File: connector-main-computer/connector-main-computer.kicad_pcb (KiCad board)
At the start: 2 copper layers, 97.3 x 100.3 mm, 42 parts, among them J1 DVI-I_Dual_Link, J10 Conn_01x04_MountingPin, J11 Conn_01x04_MountingPin, J12 Conn_01x02_MountingPin, J13 Conn_01x04_MountingPin, J2 Conn_01x03_MountingPin, J3 Conn_01x03_MountingPin, J4 Conn_01x03_MountingPin, J5 Conn_01x03_MountingPin, J6 Conn_01x03_MountingPin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

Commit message: add current divider
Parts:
- added R7: R, Resistor_SMD:R_0805_2012Metric, F.Cu at (121.9, 116.4)
- added R8: R, Resistor_SMD:R_0805_2012Metric, F.Cu at (121.9, 121.9)
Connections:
- J6 pad 1: TEST_STAND_BAT_V -> Net-(J6-Pin_1)
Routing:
- net Net-(J6-Pin_1): track 0.00 -> 10.3 mm
- net TEST_STAND_BAT_V: track 83.4 -> 76.4 mm
- net GND: track 245.0 -> 246.1 mm, vias 30 -> 31

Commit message: change strain power supply
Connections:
- J1 pad 9: +12V -> GND
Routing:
- net +12V: track 238.9 -> 236.6 mm
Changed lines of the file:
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@@
 			(layers "*.Cu" "*.Mask")
 			(remove_unused_layers no)
-			(net 3 "+12V")
+			(net 1 "GND")
 			(pinfunction "D1-")
 			(pintype "passive")
@@
 	)
 	(segment
-		(start 95.3008 53.8988)
-		(end 94.8944 53.8988)
-		(width 1)
-		(layer "B.Cu")
-		(net 3)
-	)
-	(segment
 		(start 58.166 61.8236)
 		(end 68.6816 61.8236)
@@
 	)
 	(segment
-		(start 94.8944 53.8988)
-		(end 94.4032 54.39)
-		(width 1)
-		(layer "B.Cu")
-		(net 3)
-	)
-	(segment
 		(start 95.3008 53.8988)
 		(end 95.3008 55.6768)
@@
 		(width 1)
 		(layer "B.Cu")
-		(net 3)
-	)
-	(segment
-		(start 94.4032 54.39)
-		(end 93.218 54.39)
-		(width 1)
-		(layer "B.Cu")

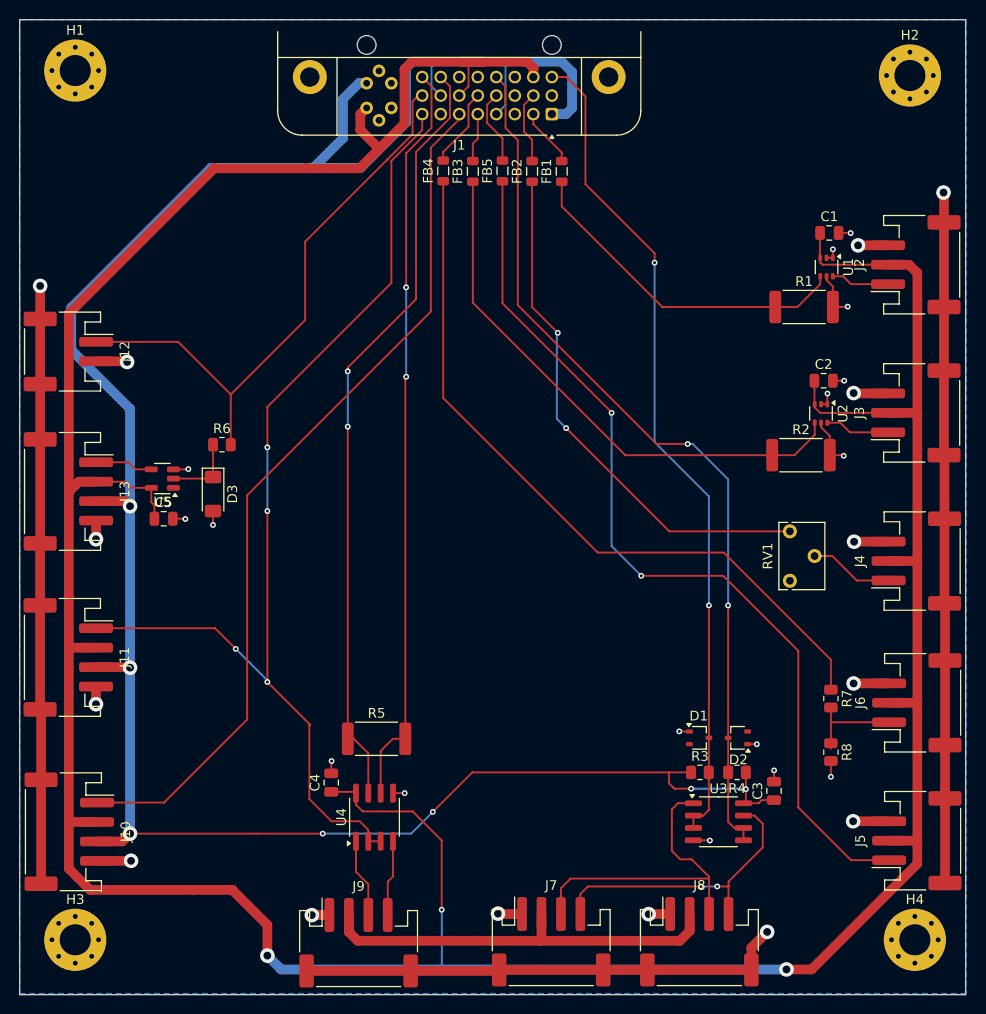
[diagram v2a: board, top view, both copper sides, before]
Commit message: Connector main computer texts and move connectors
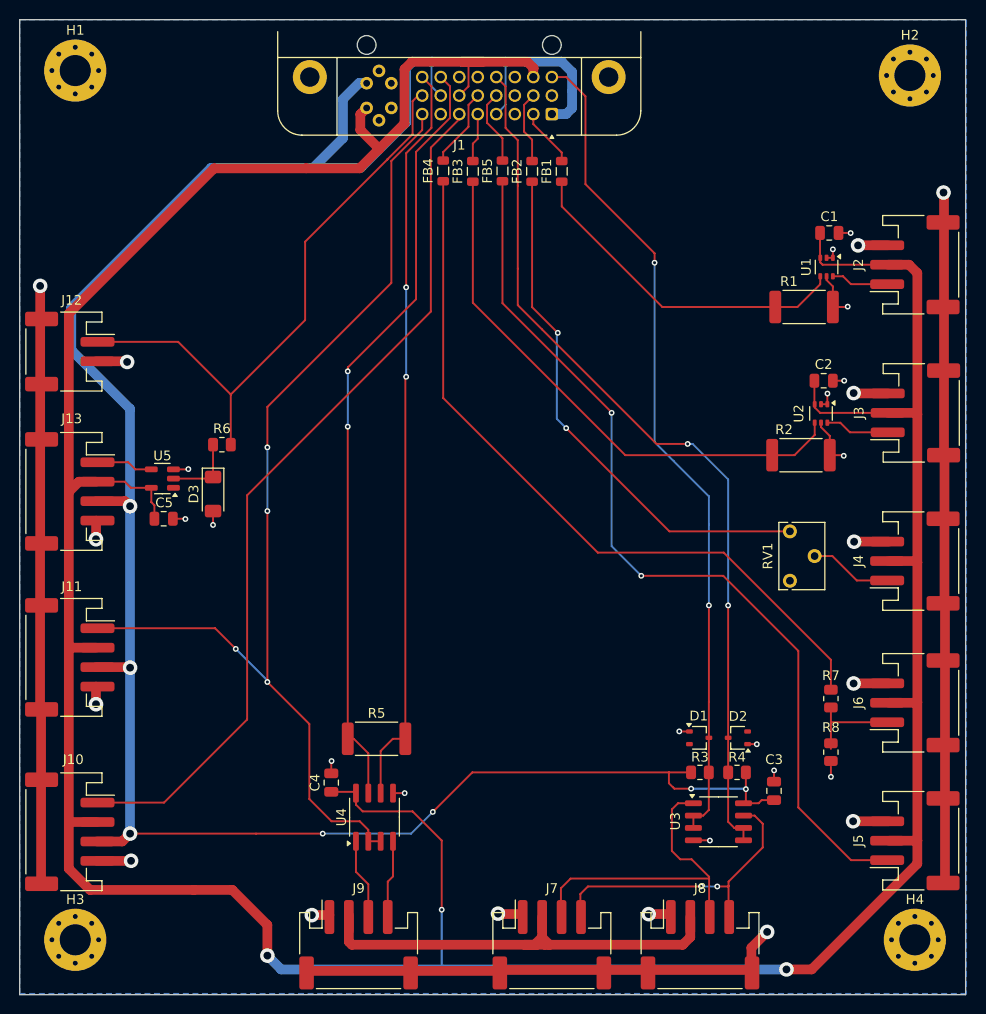
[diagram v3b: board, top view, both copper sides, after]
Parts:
- added G***: LOGO, shared:logo20x20, F.Cu at (86.1, 93.7)
- moved J7 0.32 mm to (93.2, 141.7)
- moved J8 0.32 mm to (108.5, 141.7)
- moved J9 0.21 mm to (73.3, 141.7)
- moved J5 0.20 mm to (130.6, 131.0)
- moved J6 0.20 mm to (130.6, 116.8)
- moved J11 0.15 mm to (43.6, 112.2)
- moved J4 0.15 mm to (130.6, 102.3)
- moved J12 0.14 mm to (43.6, 80.7)
- moved J13 0.14 mm to (43.6, 95.1)
- moved J2 0.10 mm to (130.6, 71.8)
- moved J10 0.05 mm to (43.6, 130.1)
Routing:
- net Net-(J7-Pin_2): track 42.1 -> 45.7 mm

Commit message: Rework main computer connector
* Add filtering for 5V and 12V lines
* Add input protection for RS485
* Run all test stand logic on 5V - add level translation
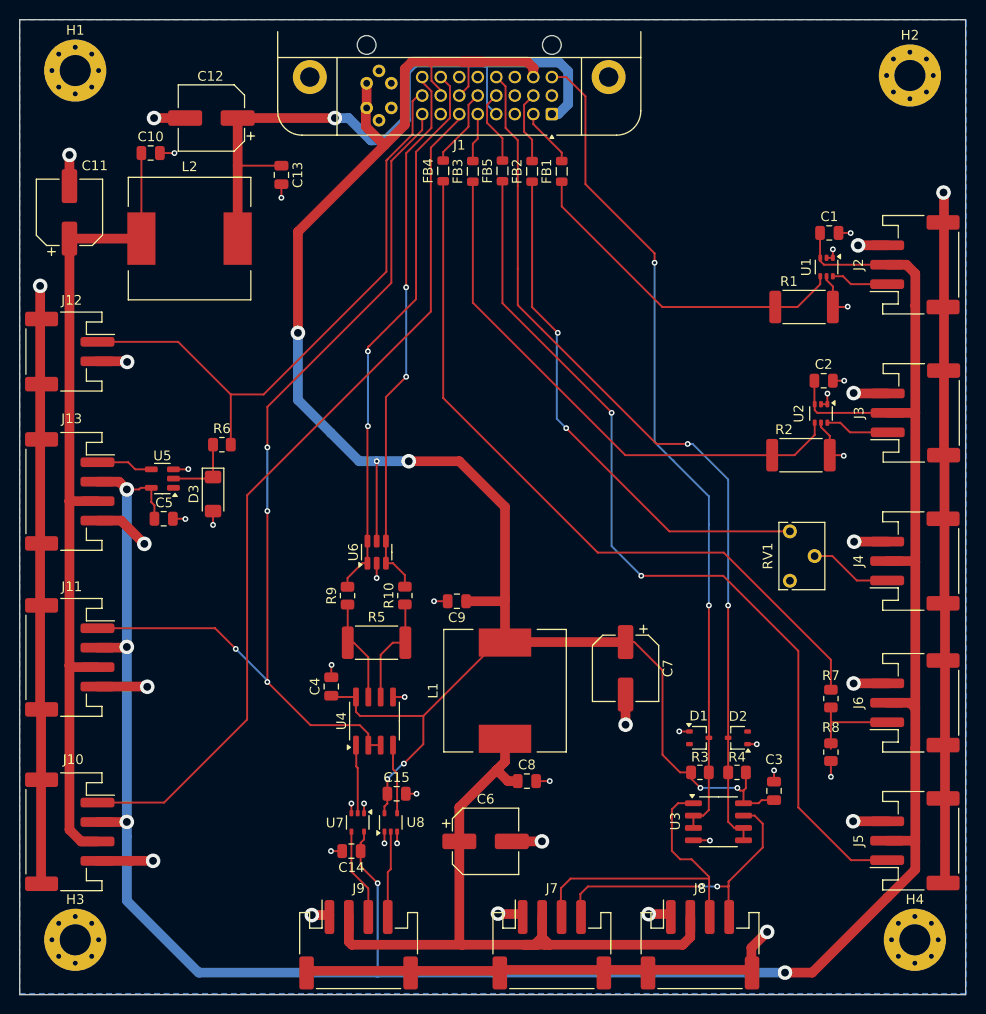
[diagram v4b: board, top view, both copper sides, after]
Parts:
- added C10: 100nF, Capacitor_SMD:C_0805_2012Metric, F.Cu at (52.0, 60.3)
- added C11: 100nF 25V, Capacitor_SMD:CP_Elec_6.3x5.8, F.Cu at (43.6, 66.4)
- added C12: 100nF 25V, Capacitor_SMD:CP_Elec_6.3x5.8, F.Cu at (58.2, 56.7)
- added C13: 100nF, Capacitor_SMD:C_0805_2012Metric, F.Cu at (65.4, 62.5)
- added C14: 100nF, Capacitor_SMD:C_0805_2012Metric, F.Cu at (72.6, 132.1)
- added C15: 100nF, Capacitor_SMD:C_0805_2012Metric, F.Cu at (77.2, 126.2)
- added C6: 100nF 16V, Capacitor_SMD:CP_Elec_6.3x5.8, F.Cu at (86.4, 131.1)
- added C7: 100nF 16V, Capacitor_SMD:CP_Elec_6.3x5.8, F.Cu at (100.8, 113.3)
- added C8: 100nF, Capacitor_SMD:C_0805_2012Metric, F.Cu at (90.7, 124.9)
- added C9: 100nF, Capacitor_SMD:C_0805_2012Metric, F.Cu at (83.5, 106.4)
- added L1: 100uH, Inductor_SMD:L_12x12mm_H8mm, F.Cu at (88.4, 115.6)
- added L2: 100uH, Inductor_SMD:L_12x12mm_H8mm, F.Cu at (56.0, 69.1)
- added R10: 10R thick film, Resistor_SMD:R_0805_2012Metric, F.Cu at (78.1, 105.8)
- added R9: 10R thick film, Resistor_SMD:R_0805_2012Metric, F.Cu at (72.2, 105.8)
- added U6: CDSOT236-0504C, Package_TO_SOT_SMD:SOT-23-6, F.Cu at (75.2, 101.4)
- added U7: SN74LV1T125DCK, Package_TO_SOT_SMD:SOT-353_SC-70-5, F.Cu at (73.2, 129.2)
- added U8: SN74LV1T125DCK, Package_TO_SOT_SMD:SOT-353_SC-70-5, F.Cu at (76.7, 129.2)
- C1, C2, C4, C5: value C -> 100nF
- C3: value C -> 100nf
- D3: value D_Zener -> 3.3V Zener
- R1, R2: value R -> 0R25
- R3, R4: value R -> 330R
- R6: value R -> 10K
- R7: value R -> 1K
- R8: value R -> 14K
- RV1: value R_Potentiometer -> 47K
- moved U4 9.89 mm to (75.0, 118.7)
- moved C4 9.89 mm to (70.5, 115.2)
- moved R5 9.89 mm to (75.2, 110.7)
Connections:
- C3 pad 1: +12V -> +5V
- C4 pad 1: +3.3V -> +5V
- J1 pad 14: +3.3V -> +5V
- J1 pad 15: +12V -> +5V
- J1 pad 18: +3.3V -> +5V
- J1 pad C2: +3.3V -> +5V
- J1 pad C4: +12V -> +5V
- J10 pad 3: +12V -> VDD
- J11 pad 3: +12V -> VDD
- J13 pad 3: +12V -> VDD
- J9 pad 3: RX -> Net-(J9-Pin_3)
- J9 pad 4: TX -> Net-(J9-Pin_4)
- R3 pad 1: +12V -> +5V
- R4 pad 1: +12V -> +5V
- R5 pad 1: RS485 bus A -> Net-(U4-B)
- R5 pad 2: RS485 bus B -> Net-(U4-A)
- U3 pad 8: +12V -> +5V
- U4 pad 6: RS485 bus B -> Net-(U4-A)
- U4 pad 7: RS485 bus A -> Net-(U4-B)
- U4 pad 8: +3.3V -> +5V
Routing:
- net +5V: track 0.00 -> 200.9 mm, vias 0 -> 7
- net +12V: track 236.6 -> 69.7 mm, vias 7 -> 1
- net +3.3V: track 372.6 -> 258.6 mm, vias 3 -> 5
- net VDD: track 0.00 -> 86.2 mm
- net GND: track 246.1 -> 282.0 mm, vias 31 -> 46
- net Net-(J7-Pin_2): track 45.7 -> 71.5 mm
- net RS485 bus A: track 79.6 -> 57.5 mm
- net RS485 bus B: track 77.0 -> 56.0 mm
- net Net-(U4-A): track 0.00 -> 11.4 mm
- net Net-(U4-B): track 0.00 -> 10.8 mm
- net Net-(J9-Pin_3): track 0.00 -> 9.50 mm
- net Net-(J9-Pin_4): track 0.00 -> 8.91 mm
- net RS485 transmit enable: track 108.7 -> 100.0 mm
- net PHYSICAL_SAFETy_SWITCH: track 60.4 -> 62.4 mm
- net RX: track 8.11 -> 7.07 mm
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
